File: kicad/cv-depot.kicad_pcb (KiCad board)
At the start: 2 copper layers, 152.3 x 128.5 mm, 205 parts, among them J1 MIDI THRU, J10 Gate 2, J11 CAN, J12 Modulation CV, J13 Bus Connector, J14 bus (controller), J2 MIDI IN, J3 MIDI, J4 MIDI, J5 Note 1, J6 bus (board), J7 Note 2, J8 Gate 1, J9 Expression CV, P1 LED Window 5mm, P10 3.5mm single channel, P11 3.5mm single channel, P12 DIN 5 pin, P13 Spacer 2M without hole, P14 Spacer 2M without hole, P15 Spacer 2M without hole, P16 Spacer 2M without hole, P2 LED Window 5mm, P3 LTC-4724JR_LTO, P4 PEL12D, P5 3.5mm single channel, P6 3.5mm single channel, P7 DIN 5 pin, P8 3.5mm single channel, P9 3.5mm single channel, Q1 BC847B, Q10 MMBFJ176, Q11 MMBFJ176, Q12 MMBFJ112, Q13 BC847B, Q14 BC847B, Q15 BC847B, Q16 BC847B, Q17 BC847B, Q18 BC847B, Q2 BC847B, Q3 BC857B, Q4 BC857B, Q5 BC847B, Q6 BC857B, Q7 BC847B, Q8 BC857B, Q9 MMBFJ112, SW1 Reset, U1 PEL12D-4225S-S2024, U10 LMV324A, U11 SN65HVD1050D, U12 MCP4011-103E/SN, U13 TL074, U14 MCP4011-503E/SN, U2 6N138, U3 TL074, U5 REF3030, U6 DG419LDY, U7 MCP4011-103E/SN, U8 TL072, U9 MCP4011-503E/SN

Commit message: tweaked the PCB design
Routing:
- net +5V-3: track 61.2 -> 60.1 mm
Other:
- board text added: "CV Depot"
- board text removed: "CV Fountain"

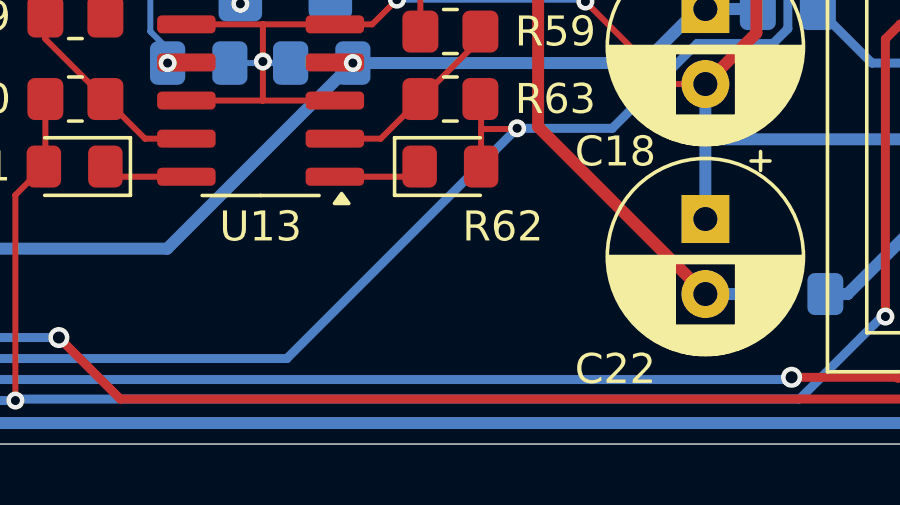
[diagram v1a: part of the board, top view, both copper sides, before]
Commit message: done with initial hardware check except voltage outputs
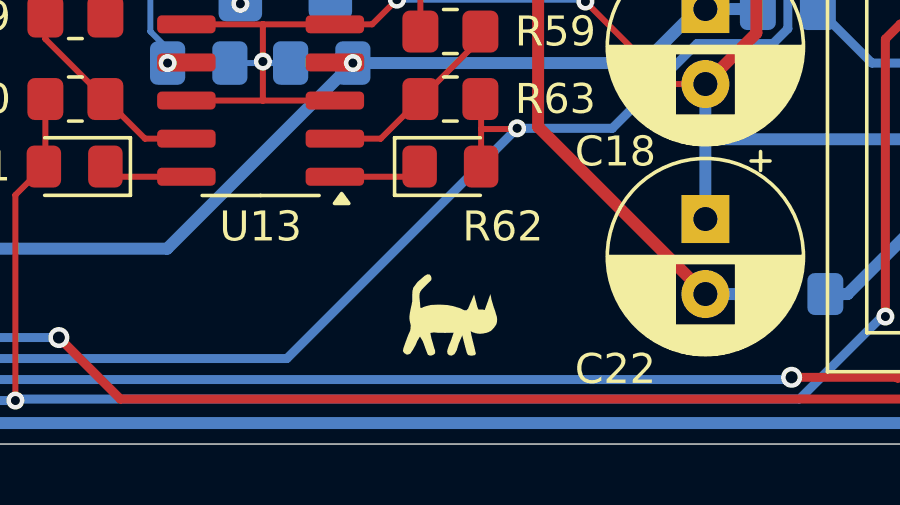
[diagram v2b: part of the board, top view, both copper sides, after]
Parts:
- added REF**: SilkScreenSmall, GajeLogo:SilkScreenSmall, F.Cu at (143.5, 148.8)
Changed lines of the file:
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@@
 		(tenting front back)
 		(pcbplotparams
-			(layerselection 0x00000000_00000000_55555555_5755f5ff)
+			(layerselection 0x00000000_00000000_55555555_575555ff)
 			(plot_on_all_layers_selection 0x00000000_00000000_00000000_00000000)
 			(disableapertmacros no)
-			(usegerberextensions no)
+			(usegerberextensions yes)
 			(usegerberattributes no)
 			(usegerberadvancedattributes no)
@@
 			(drillshape 0)
 			(scaleselection 1)
-			(outputdirectory "")
+			(outputdirectory "fusionpcb")
 		)
 	)
@@
 			(at 0 1.65 90)
 			(layer "F.Fab")
-			(hide yes)
 			(effects
 				(font
@@
 		)
 	)
+	(footprint "GajeLogo:SilkScreenSmall"
+		(layer "F.Cu")
+		(at 143.5 148.75)
+		(property "Reference" "REF**"
+			(at -5.334 -1.016 0)
+			(unlocked yes)
+			(layer "F.SilkS")
+			(hide yes)
+			(effects
+				(font
+					(size 1 1)
+					(thickness 0.1)
+				)
+			)
+		)
+		(property "Value" "SilkScreenSmall"
+			(at -1.778 -5.334 0)
+			(unlocked yes)
+			(layer "F.Fab")
+			(hide yes)
+			(effects
+				(font
+					(size 1 1)
+					(thickness 0.15)
+				)
+			)
+		)
+		(property "Datasheet" ""
+			(at -8.89 -13.216 0)
+			(unlocked yes)
+			(layer "F.Fab")
+			(hide yes)
+			(effects
+				(font
+					(size 1 1)
+					(thickness 0.15)
+				)
+			)
+		)
+		(property "Description" ""
+			(at -8.89 -13.216 0)
+			(unlocked yes)
+			(layer "F.Fab")
+			(hide yes)
+			(effects
+				(font
+					(size 1 1)
+					(thickness 0.15)
+				)
+			)
+		)
+		(attr smd)
+		(fp_poly
+			(pts
+				(xy -1.27 -0.508) (xy -1.27 -0.762) (xy -1.261493 -0.864187) (xy -1.233226 -0.966976) (xy -1.094278 -1.153843)
+				(xy -0.85144 -1.361991) (xy -0.762784 -1.408246) (xy -0.689547 -1.400536) (xy -0.643292 -1.338863)
+				(xy -0.627874 -1.269481) (xy -0.639438 -1.207808) (xy -0.770494 -1.084461) (xy -0.955513 -0.895587)
+				(xy -1.001768 -0.826204) (xy -1.024896 -0.764531) (xy -1.032605 -0.652748) (xy -1.009477 -0.429183)
+				(xy -1.001768 -0.301982) (xy -0.974786 -0.282709) (xy -0.836021 -0.340527) (xy -0.643292 -0.386782)
+				(xy -0.365763 -0.398346) (xy -0.088233 -0.382928) (xy 0.10064 -0.344382) (xy 0.301078 -0.286563)
+				(xy 0.432134 -0.22489) (xy 0.466825 -0.209472) (xy 0.536207 -0.209472) (xy 0.590172 -0.263436) (xy 0.79061 -0.737549)
+				(xy 0.902392 -0.305836) (xy 0.937084 -0.236454) (xy 0.973703 -0.232599) (xy 1.010406 -0.233826)
+				(xy 1.045013 -0.2326) (xy 1.078424 -0.232303) (xy 1.112468 -0.226817) (xy 1.145231 -0.217181) (xy 1.233886 -0.463874)
+				(xy 1.334105 -0.752967) (xy 1.372651 -0.560238) (xy 1.434324 -0.348237) (xy 1.495998 -0.170926)
+				(xy 1.549962 0.014093) (xy 1.558988 0.090464) (xy 1.555562 0.15385) (xy 1.546107 0.206822) (xy 1.530689 0.260786)
+				(xy 1.485323 0.33373) (xy 1.437355 0.391977) (xy 1.387673 0.445085) (xy 1.343722 0.482034) (xy 1.261311 0.523357)
+				(xy 1.203695 0.543095) (xy 1.071994 0.569152) (xy 1.008394 0.573006) (xy 0.94611 0.572857) (xy 0.896611 0.567225)
+				(xy 0.848428 0.557588) (xy 0.755918 0.530606) (xy 0.674972 0.488206) (xy 0.713518 0.673226) (xy 0.829155 1.143484)
+				(xy 0.852283 1.243703) (xy 0.817592 1.286104) (xy 0.709664 1.305377) (xy 0.60559 1.289958) (xy 0.578608 1.266831)
+				(xy 0.547771 1.209012) (xy 0.493807 1.012429) (xy 0.397443 0.626971) (xy 0.274096 0.91221) (xy 0.212423 1.120357)
+				(xy 0.139186 1.251412) (xy 0.038967 1.305377) (xy -0.045833 1.286104) (xy -0.092088 1.239849) (xy -0.107506 1.166612)
+				(xy -0.092088 1.08952) (xy -0.049687 0.962319) (xy 0.015839 0.808136) (xy 0.108349 0.538315) (xy -0.165325 0.546025)
+				(xy -0.415872 0.54217) (xy -0.546928 0.530606) (xy -0.66642 0.546025) (xy -0.635583 0.711771) (xy -0.589328 0.873664)
+				(xy -0.546928 1.020138) (xy -0.508382 1.13963) (xy -0.508382 1.22443) (xy -0.558492 1.270685) (xy -0.620165 1.297667)
+				(xy -0.689547 1.301522) (xy -0.747366 1.27454) (xy -0.793621 1.170466) (xy -0.882276 0.919919) (xy -0.920822 0.8197)
+				(xy -1.013332 0.665517) (xy -1.101987 0.811991) (xy -1.155951 0.943046) (xy -1.240752 1.097229)
+				(xy -1.325553 1.22443) (xy -1.353117 1.245373) (xy -1.383953 1.257365) (xy -1.417836 1.266692) (xy -1.466375 1.264788)
+				(xy -1.537555 1.220576) (xy -1.58381 1.151193) (xy -1.568391 1.066393) (xy -1.495154 0.854391) (xy -1.406499 0.619262)
+				(xy -1.340971 0.476642) (xy -1.329407 0.399551) (xy -1.321698 0.287768) (xy -1.3489 0.176621) (xy -1.364511 0.083115)
+				(xy -1.364319 0.00188) (xy -1.359179 -0.056367) (xy -1.350613 -0.119754) (xy -1.329407 -0.22489)
+			)
+			(stroke
+				(width 0)
+				(type solid)
+			)
+			(fill yes)
+			(layer "F.SilkS")
+		)
+		(embedded_fonts no)
+	)
 	(footprint "Package_TO_SOT_SMD:SOT-23"
 		(layer "F.Cu")
@@
 			(at 0 2.4 90)
 			(layer "F.Fab")
-			(hide yes)
 			(effects
 				(font
@@
 			(at 4.3125 0.95 0)
 			(layer "F.Fab")
-			(hide yes)
 			(effects
 				(font
@@
 			(at 0 1.65 0)
 			(layer "F.Fab")
-			(hide yes)
 			(effects
 				(font
